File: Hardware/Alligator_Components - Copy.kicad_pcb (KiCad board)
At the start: 4 copper layers, 60 x 110 mm, 122 parts, among them J1 SWD_Header, J2 Eurorack_10_pin_power, J3 Conn_01x08_Male, J4 Conn_01x08_Male, J5 Conn_01x08_Male, J6 Conn_01x08_Male, J7 USB_B_Micro, U1 STM32H743ZITx, U2 IS42S16400J-xC, U3 PCM5100APW, U4 SSI2164, U5 MCP6004, U6 MCP6004, U7 TL074, U8 LM1117-3.3, Y1 8MHz 20pF

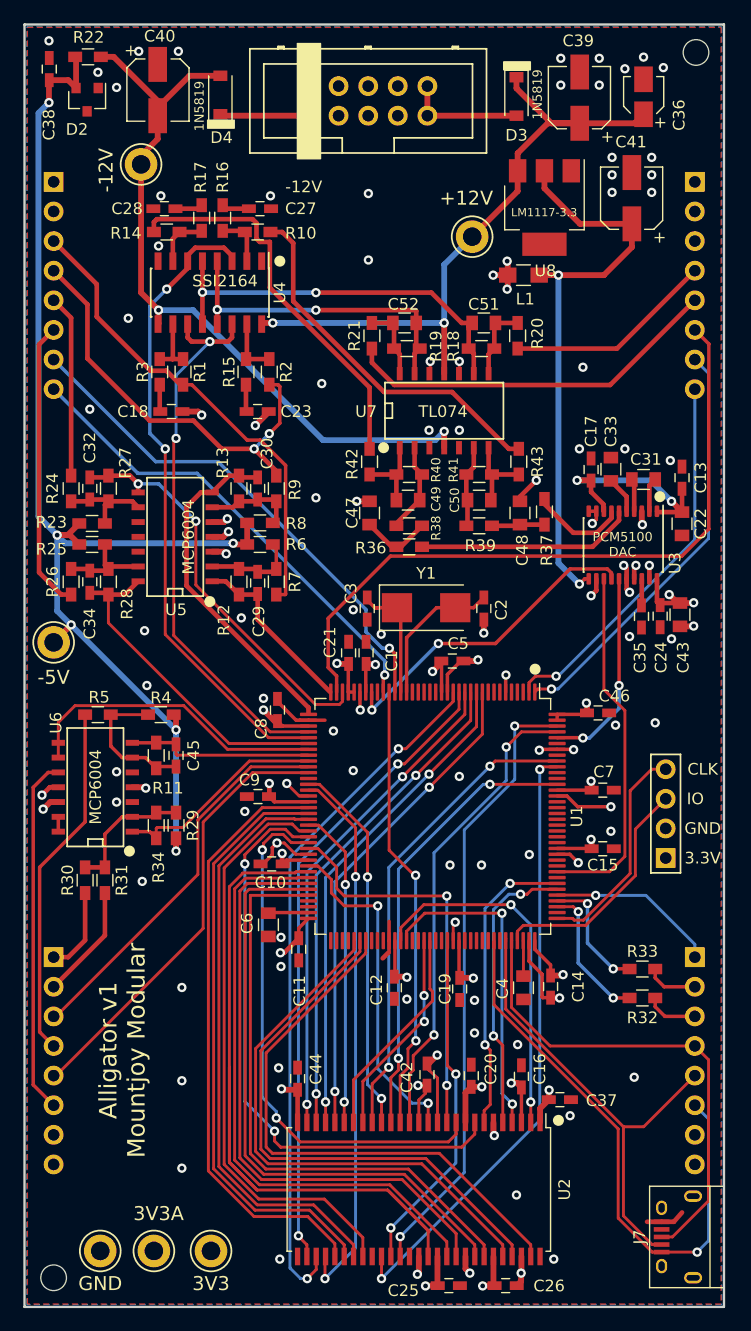
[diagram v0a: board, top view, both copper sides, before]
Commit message: Control PCB orientation tests
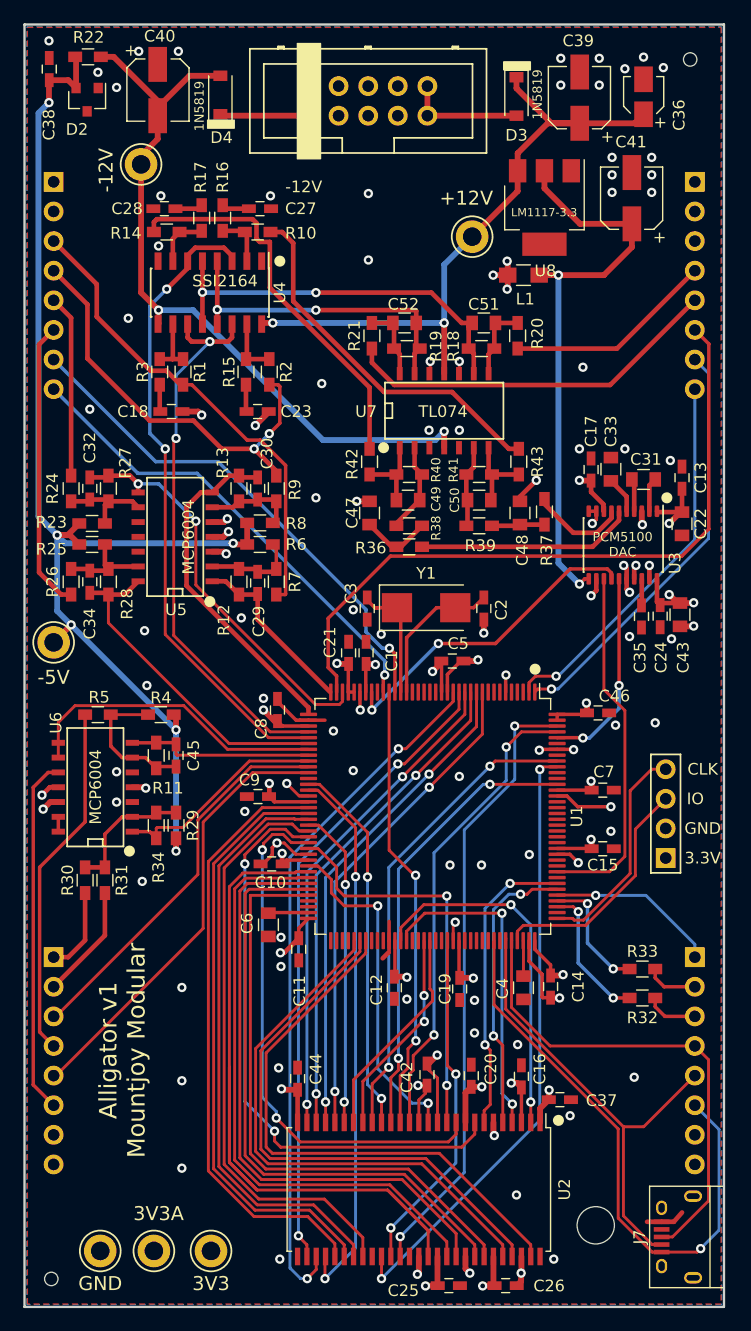
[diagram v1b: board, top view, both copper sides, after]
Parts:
- removed H2: JLC_Tooling_Hole, Custom_Footprints:JLC_SMT_Tooling_Hole
- added JLC_Tooling: MountingHole_2.2mm_M2, Mounting_Holes:MountingHole_2.2mm_M2, F.Cu at (102.3, 157.6)
- added JLC_Tooling: MountingHole_2.2mm_M2, Mounting_Holes:MountingHole_2.2mm_M2, F.Cu at (157.1, 53.0)
- H1: value JLC_Tooling_Hole -> MountingHole_Pad; footprint Custom_Footprints:JLC_SMT_Tooling_Hole -> Mounting_Holes:MountingHole_3.2mm_M3
- J3, J4, J5, J6: value Conn_01x08_Male -> Conn_01x08_Female
- moved H1 101.0 mm to (149.0, 153.0)
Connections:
- H1 pad 1: (no net) -> GND
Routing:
- net +3.3VA: track 30.3 -> 21.5 mm
- net /USB_VBUS: track 49.7 -> 50.4 mm
